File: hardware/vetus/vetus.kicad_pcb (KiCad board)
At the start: 2 copper layers, 75 x 80 mm, 51 parts, among them J1 anemo, J2 Conn_01x05_Male, J3 RJ45, J4 Term_sel, U1 NSI45020T1G, U10 LM4040DBZ-2.0, U11 MCP4706, U12 MCP2542FDxMF, U13 uA7805, U2 NSI45020T1G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

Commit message: Modifications mineures pour fabrication
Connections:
- net Net-(J3-Pad1) renamed /CANH
- net Net-(J3-Pad2) renamed /CANL

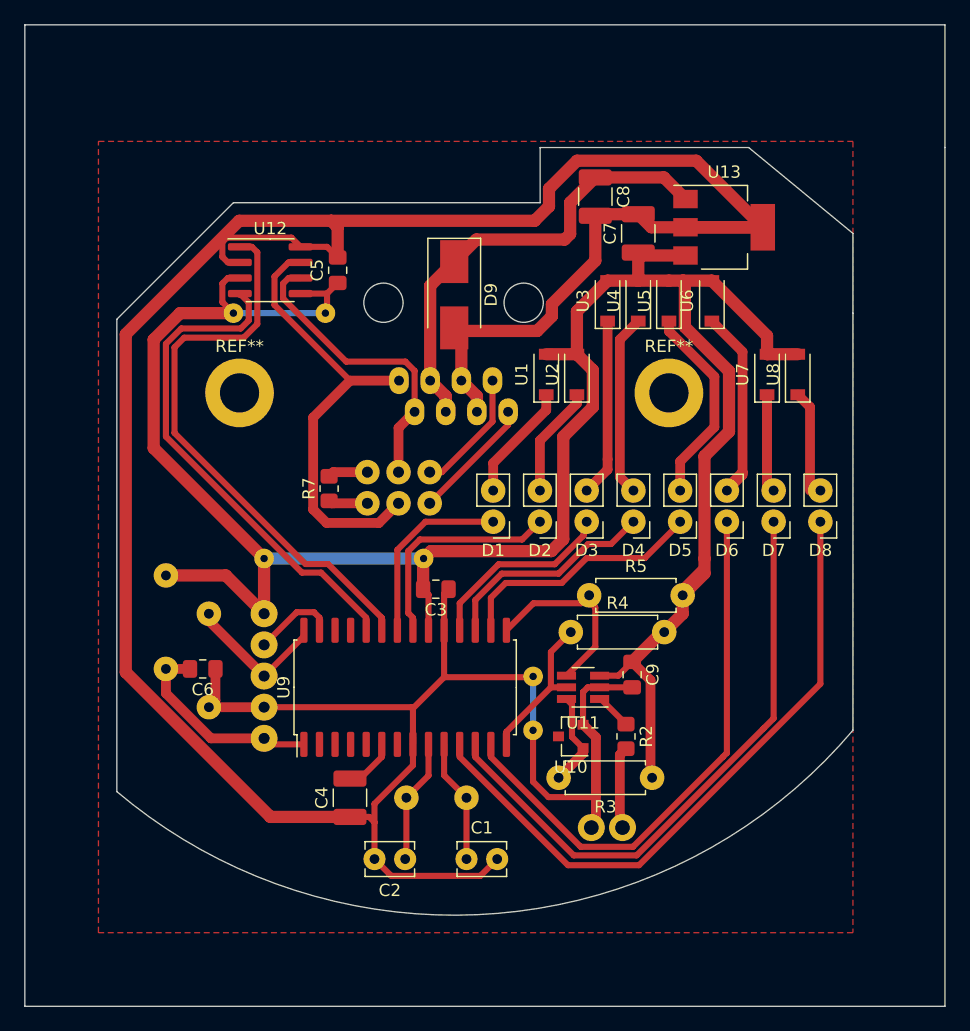
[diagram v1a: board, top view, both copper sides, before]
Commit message: Convert power and vetus to new kicad format
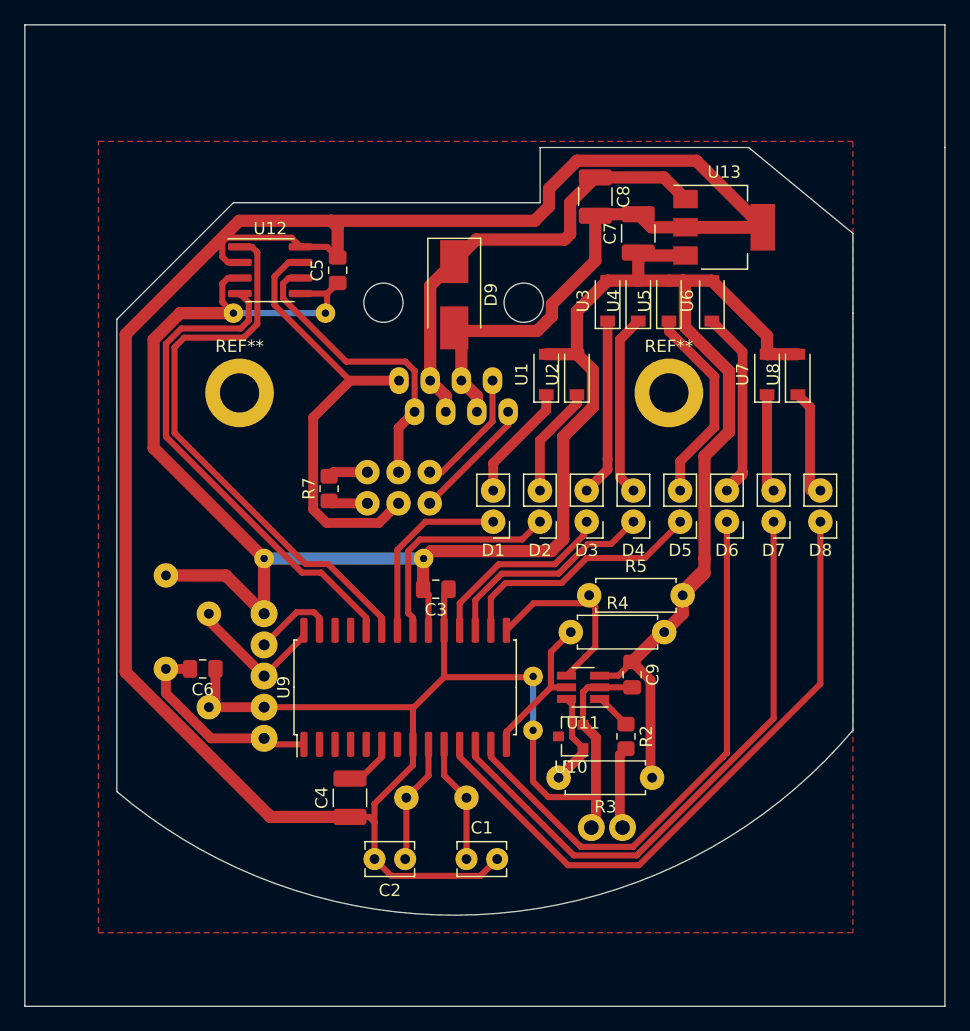
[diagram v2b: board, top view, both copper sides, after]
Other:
- net class Default removed
